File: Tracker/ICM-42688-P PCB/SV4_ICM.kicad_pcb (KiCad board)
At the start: 2 copper layers, 17.8 x 26.5 mm, 22 parts, among them U1 SuperMini nRF52840, U2 ICM-42688-P, U3 MMC5983MA, U4 K3-1295S-E1

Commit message: - Moved resistor to avoid conflict with USB C port - Added PDF of schematic for SlimeVR Marketplace listing
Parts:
- moved R1 3.19 mm to (148.9, 79.9), turned to 180 degrees
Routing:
- net +3V3: track 53.3 -> 53.9 mm
- net SCL: track 26.7 -> 27.2 mm

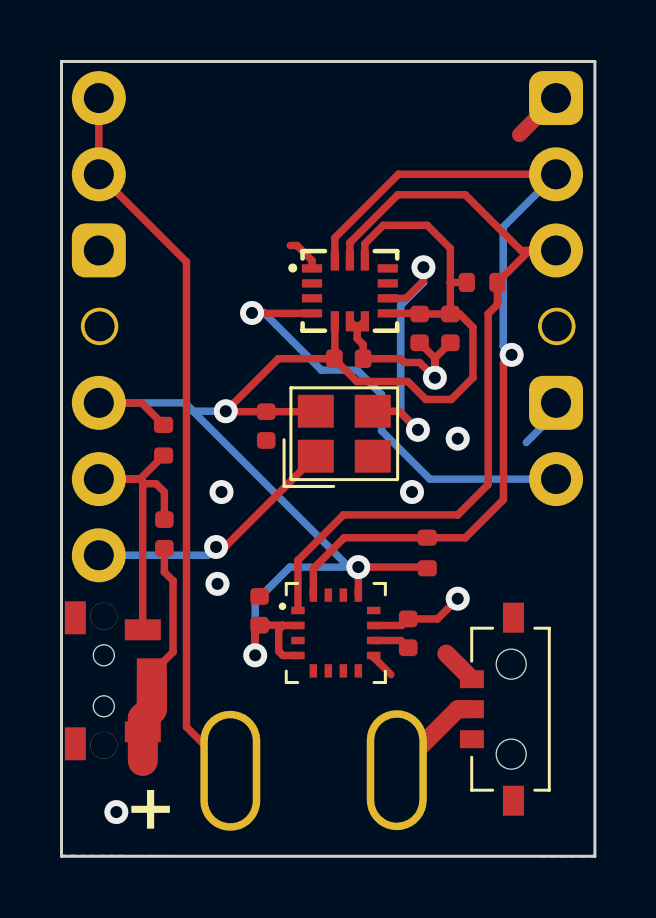
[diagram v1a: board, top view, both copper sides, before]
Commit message: - Added testing jig 3d model - Added folder for jigs - Removed debouncing capacitor from PCB, not needed.
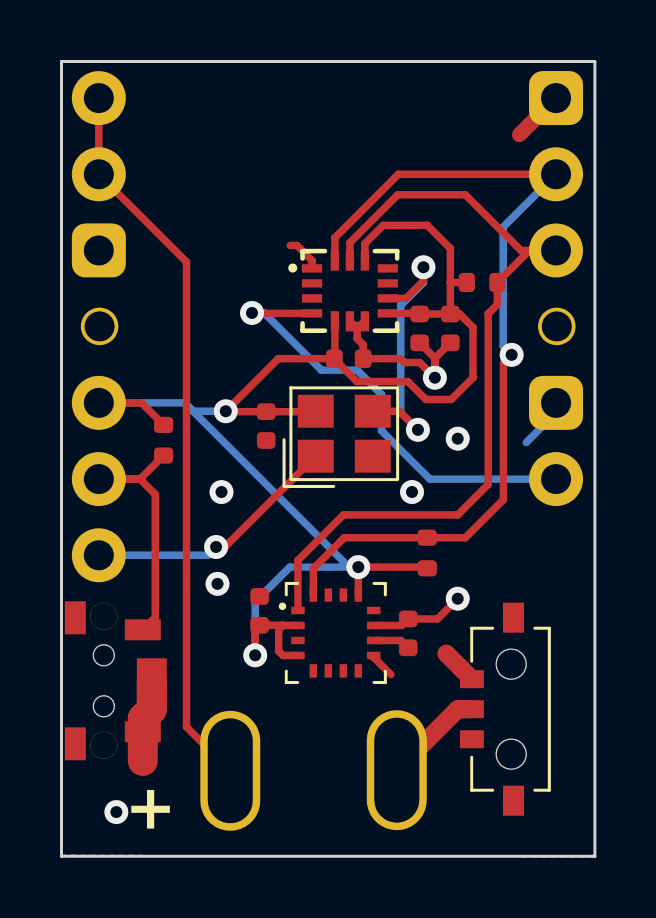
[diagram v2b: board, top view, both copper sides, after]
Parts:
- removed C1: 100nF, Capacitor_SMD:C_0402_1005Metric
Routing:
- net GND: track 25.1 -> 20.2 mm
- net Net-(U1-P0.31-LF): track 10.7 -> 9.26 mm
